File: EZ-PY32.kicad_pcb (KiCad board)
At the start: 2 copper layers, 1 part, among them U2 3.5

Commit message: i did everithing
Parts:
- removed U2: 3.5, EZ-PY32:kuman_display_3.5zoll
- added U4: 3.5, EZ-PY32:kuman_display_3.5zoll, F.Cu at (59.6, 114.6)
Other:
- net class Default: clearance 0.2 -> 0.1524; trace_width 0.25 -> 0.3; via_dia 0.8 -> 0.6; via_drill 0.4 -> 0.3
- net class Power added: clearance 0.1524, trace_width 0.5, via_dia 0.6, via_drill 0.3
- rule trace_clearance: 0.2 -> 0.1524

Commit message: logo einfügen
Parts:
- added G***: LOGO, EZ-PY32:EZ, B.Cu at (109.0, 90.8)
- added G***: LOGO, EZ-PY32:OTH_3000x3000dpi, B.Cu at (125.6, 89.7)

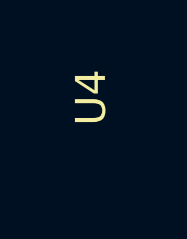
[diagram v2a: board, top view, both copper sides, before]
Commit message: relocating display
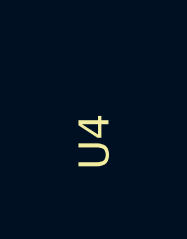
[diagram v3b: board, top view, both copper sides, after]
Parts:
- removed G***: LOGO, EZ-PY32:EZ
- removed G***: LOGO, EZ-PY32:OTH_3000x3000dpi
- moved U4 1.48 mm to (59.8, 116.0)

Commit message: smal fixes
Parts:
- added U3: ESP32-WROOM-32, RF_Module:ESP32-WROOM-32, F.Cu at (71.1, 108.9)
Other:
- rule trace_min: 0.2 -> 0

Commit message: Add CAD
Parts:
- removed U4: 3.5, EZ-PY32:kuman_display_3.5zoll
- added C2: 10nF, Capacitor_SMD:C_0603_1608Metric_Pad1.08x0.95mm_HandSolder, F.Cu at (128.0, 123.3)
- added J3: Conn_02x08_Odd_Even, EZ-PY32:HTSS-108-01-YY-DV, B.Cu at (71.0, 78.2)
- added U6: 3.5, EZ-PY32:kuman_display_3.5zoll, F.Cu at (59.8, 116.0)
- renumbered U3 to U5
